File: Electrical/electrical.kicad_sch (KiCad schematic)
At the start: 6 parts, among them SW1 SW_Push

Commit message: Circuit planing
First final version of circuit
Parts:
- added D4: LED, symbol Device:LED
- added M1, M2: Motor_DC, symbol Motor:Motor_DC
- added R2: 10kOhm, symbol Device:R
- added SW2: SW_Push, symbol Switch:SW_Push
- added SW3: SW_DPST_x2, symbol Switch:SW_DPST_x2
- added U1: MPXA6115A, symbol Sensor_Pressure:MPXA6115A
- added U2: L298N, Package_TO_SOT_THT:TO-220-15_P2.54x2.54mm_StaggerOdd_Lead4.58mm_Vertical, symbol Driver_Motor:L298N
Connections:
- net at A1.15 (D0/RX): now also U2.5 (IN1)
- net at A1.16 (D1/TX): now also U2.7 (IN2)
- net at A1.17 (D2): now also U2.10 (IN3)
- net at A1.18 (D3): now also U2.12 (IN4)
- net at A1.19 (D4): now also U2.6 (EnA)
- net at A1.20 (D5): now also U2.11 (EnB)
- net at A1.3 (~{RESET}): now also R2.2, SW2.1
- net at A1.5 (+5V), SW1.2: now also SW2.2, U1.2 (Vcc)
- net at R1.1: now also A1.7 (GND), R2.1, U1.3 (GND); no longer A1.6 (GND)
- net at A1.8 (VIN): now also D4.1 (K)
- net at A1.9 (A0): now also U1.4 (Vout)
- new net: M2.1 (+), U2.13 (OUT3)
- new net: M2.2 (-), U2.14 (OUT4)
- new net: SW3.2 (B), U2.9 (Vss)
- new net: M1.1 (+), U2.2 (OUT1)
- new net: M1.2 (-), U2.3 (OUT2)
- new net: D4.2 (A), U2.4 (Vs)
- new net +BATT: SW3.1 (A)
- new net GND: A1.6 (GND), U2.8 (GND)
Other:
- moved on the sheet: A1, D1, D2, D3, R1, SW1

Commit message: Konverting to Pico
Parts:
- removed A1: Arduino_UNO_R2, Module:Arduino_UNO_R2, symbol MCU_Module:Arduino_UNO_R2
- removed U1: MPXA6115A, symbol Sensor_Pressure:MPXA6115A
- added U1: Pico, RPi_Pico:RPi_Pico_SMD_TH, symbol MCU_RaspberryPi_and_Boards:Pico
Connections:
- net GND: now also U1.13 (GND)
- net at R1.1, R2.1: now also U1.3 (GND)
- net at D1.1 (K), D2.1 (K), D3.1 (K): now also U1.38 (GND)
- net at D3.2 (A): now also U1.26 (GPIO20)
- net at SW1.2, SW2.2: now also U1.36 (3V3)
- net at R1.2, SW1.1: now also U1.21 (GPIO16)
- net at D1.2 (A): now also U1.24 (GPIO18)
- net at D2.2 (A): now also U1.25 (GPIO19)
- net at D4.1 (K): now also U1.39 (VSYS)
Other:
- note added: "Main control circuitry"
- note added: "arduino control circuitry"
- moved on the sheet: D1, D2, D3

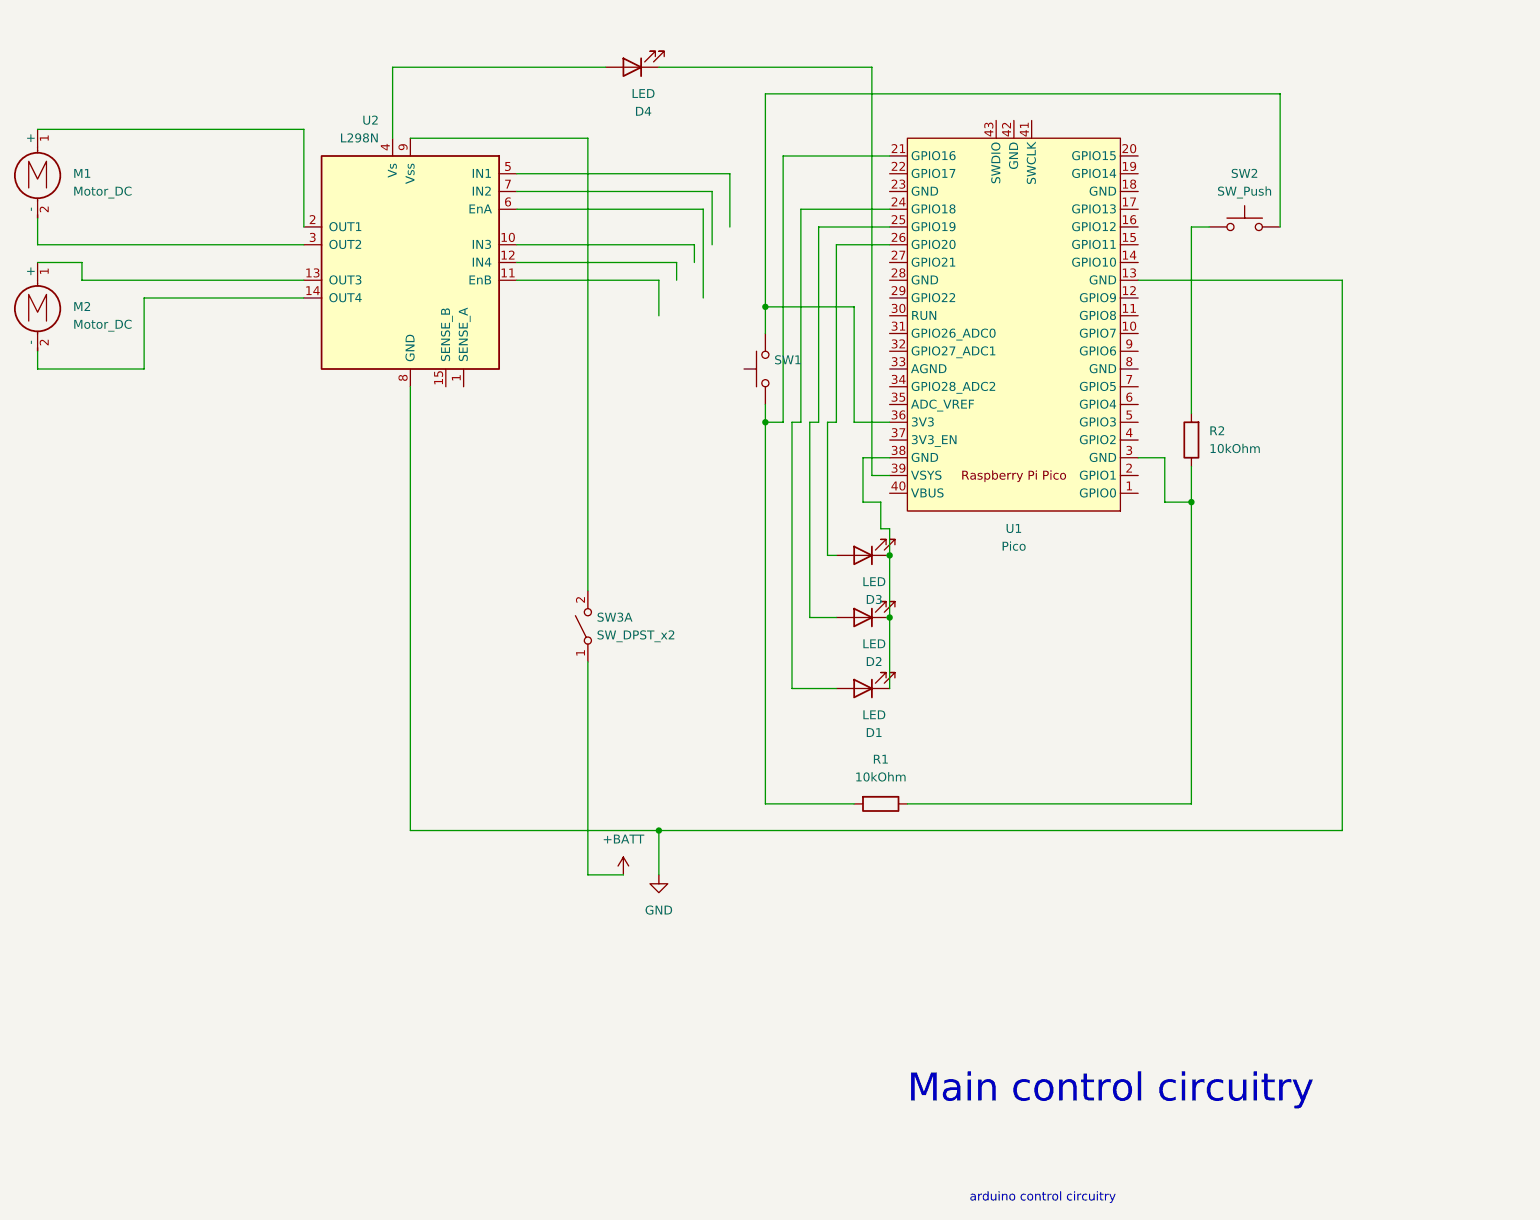
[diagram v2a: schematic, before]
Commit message: converting to a pico
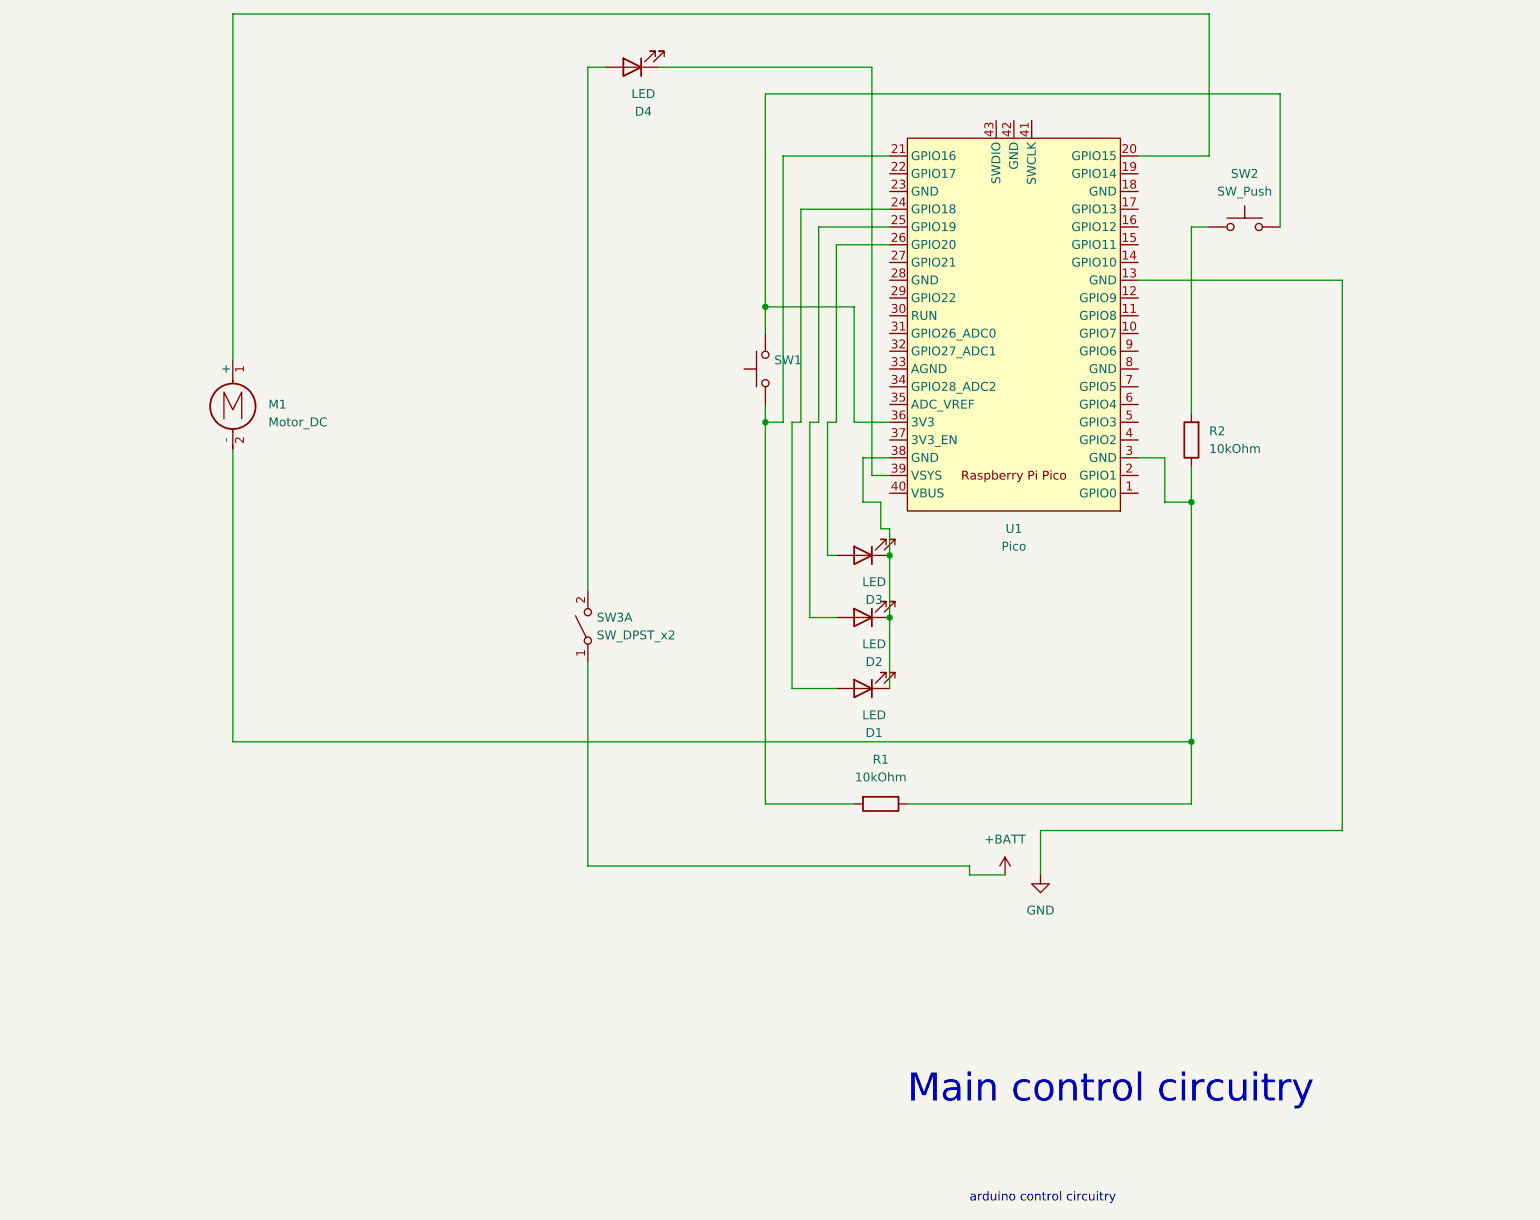
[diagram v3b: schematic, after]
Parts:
- removed M2: Motor_DC, symbol Motor:Motor_DC
- removed U2: L298N, Package_TO_SOT_THT:TO-220-15_P2.54x2.54mm_StaggerOdd_Lead4.58mm_Vertical, symbol Driver_Motor:L298N
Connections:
- net at R1.1, R2.1, U1.3 (GND): now also M1.2 (-)
- net at SW3.2 (B): now also D4.2 (A)
- net at U1.20 (GPIO15): now also M1.1 (+)

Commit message: Intro of Pico Code
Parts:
- added R3, R4, R5: R_Small, symbol Device:R_Small
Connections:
- net at D3.2 (A): now also R3.2; no longer U1.26 (GPIO20)
- net at U1.24 (GPIO18): now also R5.1; no longer D1.2 (A)
- net at U1.25 (GPIO19): now also R4.1; no longer D2.2 (A)
- new net: R3.1, U1.26 (GPIO20)
- new net: D1.2 (A), R5.2
- new net: D2.2 (A), R4.2
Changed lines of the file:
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@@
     (stroke (width 0) (type default))
   )
-  (wire (pts (xy 165.1 78.74) (xy 165.1 106.68))
+  (wire (pts (xy 165.1 78.74) (xy 165.1 100.33))
     (stroke (width 0) (type default))
   )
@@
     (stroke (width 0) (type default))
   )
-  (wire (pts (xy 167.64 78.74) (xy 167.64 97.79))
+  (wire (pts (xy 167.64 78.74) (xy 167.64 90.17))
     (stroke (width 0) (type default))
   )
@@
     (stroke (width 0) (type default))
   )
+  (wire (pts (xy 167.64 95.25) (xy 167.64 97.79))
+    (stroke (width 0) (type default))
+  )
   (wire (pts (xy 165.1 78.74) (xy 166.37 78.74))
     (stroke (width 0) (type default))
@@
     (stroke (width 0) (type default))
   )
-  (wire (pts (xy 162.56 78.74) (xy 162.56 116.84))
+  (wire (pts (xy 162.56 78.74) (xy 162.56 109.22))
+    (stroke (width 0) (type default))
+  )
+  (wire (pts (xy 165.1 105.41) (xy 165.1 106.68))
     (stroke (width 0) (type default))
   )
@@
   )
   (wire (pts (xy 193.04 143.51) (xy 187.96 143.51))
+    (stroke (width 0) (type default))
+  )
+  (wire (pts (xy 162.56 114.3) (xy 162.56 116.84))
     (stroke (width 0) (type default))
   )
@@
         )
       )
+    )
+  )
+  (symbol (lib_id "Device:R_Small") (at 167.64 92.71 0) (unit 1)
+    (in_bom yes) (on_board yes) (dnp no) (fields_autoplaced)
+    (property "Reference" "R3" (at 170.18 91.44 0)
+      (effects (font (size 1.27 1.27)) (justify left))
+    )
+    (property "Value" "R_Small" (at 170.18 93.98 0)
+      (effects (font (size 1.27 1.27)) (justify left))
+    )
+    (property "Footprint" "" (at 167.64 92.71 0)
+      (effects (font (size 1.27 1.27)) hide)
+    )
+    (property "Datasheet" "~" (at 167.64 92.71 0)
+      (effects (font (size 1.27 1.27)) hide)
+    )
+    (pin "1")
+    (pin "2")
+    (instances
+      (project "electrical"
+        (path "/a8f1ef9d-ede4-4b5c-88d3-ab957278c1f8"
+          (reference "R3") (unit 1)
+        )
+      )
+    )
+  )
+  (symbol (lib_id "Device:R_Small") (at 162.56 111.76 0) (unit 1)
+    (in_bom yes) (on_board yes) (dnp no) (fields_autoplaced)
+    (property "Reference" "R5" (at 165.1 110.49 0)
+      (effects (font (size 1.27 1.27)) (justify left))
+    )
+    (property "Value" "R_Small" (at 165.1 113.03 0)
+      (effects (font (size 1.27 1.27)) (justify left))
+    )
+    (property "Footprint" "" (at 162.56 111.76 0)
+      (effects (font (size 1.27 1.27)) hide)
+    )
+    (property "Datasheet" "~" (at 162.56 111.76 0)
+      (effects (font (size 1.27 1.27)) hide)
+    )
+    (pin "1")
+    (pin "2")
+    (instances
+      (project "electrical"
+        (path "/a8f1ef9d-ede4-4b5c-88d3-ab957278c1f8"
+          (reference "R5") (unit 1)
+        )
+      )
+    )
+  )
+  (symbol (lib_id "Device:R_Small") (at 165.1 102.87 0) (unit 1)
+    (in_bom yes) (on_board yes) (dnp no) (fields_autoplaced)
+    (property "Reference" "R4" (at 167.64 101.6 0)
+      (effects (font (size 1.27 1.27)) (justify left))
+    )
+    (property "Value" "R_Small" (at 167.64 104.14 0)
+      (effects (font (size 1.27 1.27)) (justify left))
+    )
+    (property "Footprint" "" (at 165.1 102.87 0)
+      (effects (font (size 1.27 1.27)) hide)
+    )
+    (property "Datasheet" "~" (at 165.1 102.87 0)
+      (effects (font (size 1.27 1.27)) hide)
+    )
+    (pin "1")
+    (pin "2")
+    (instances
+      (project "electrical"
+        (path "/a8f1ef9d-ede4-4b5c-88d3-ab957278c1f8"
+          (reference "R4") (unit 1)
+        )
+      )

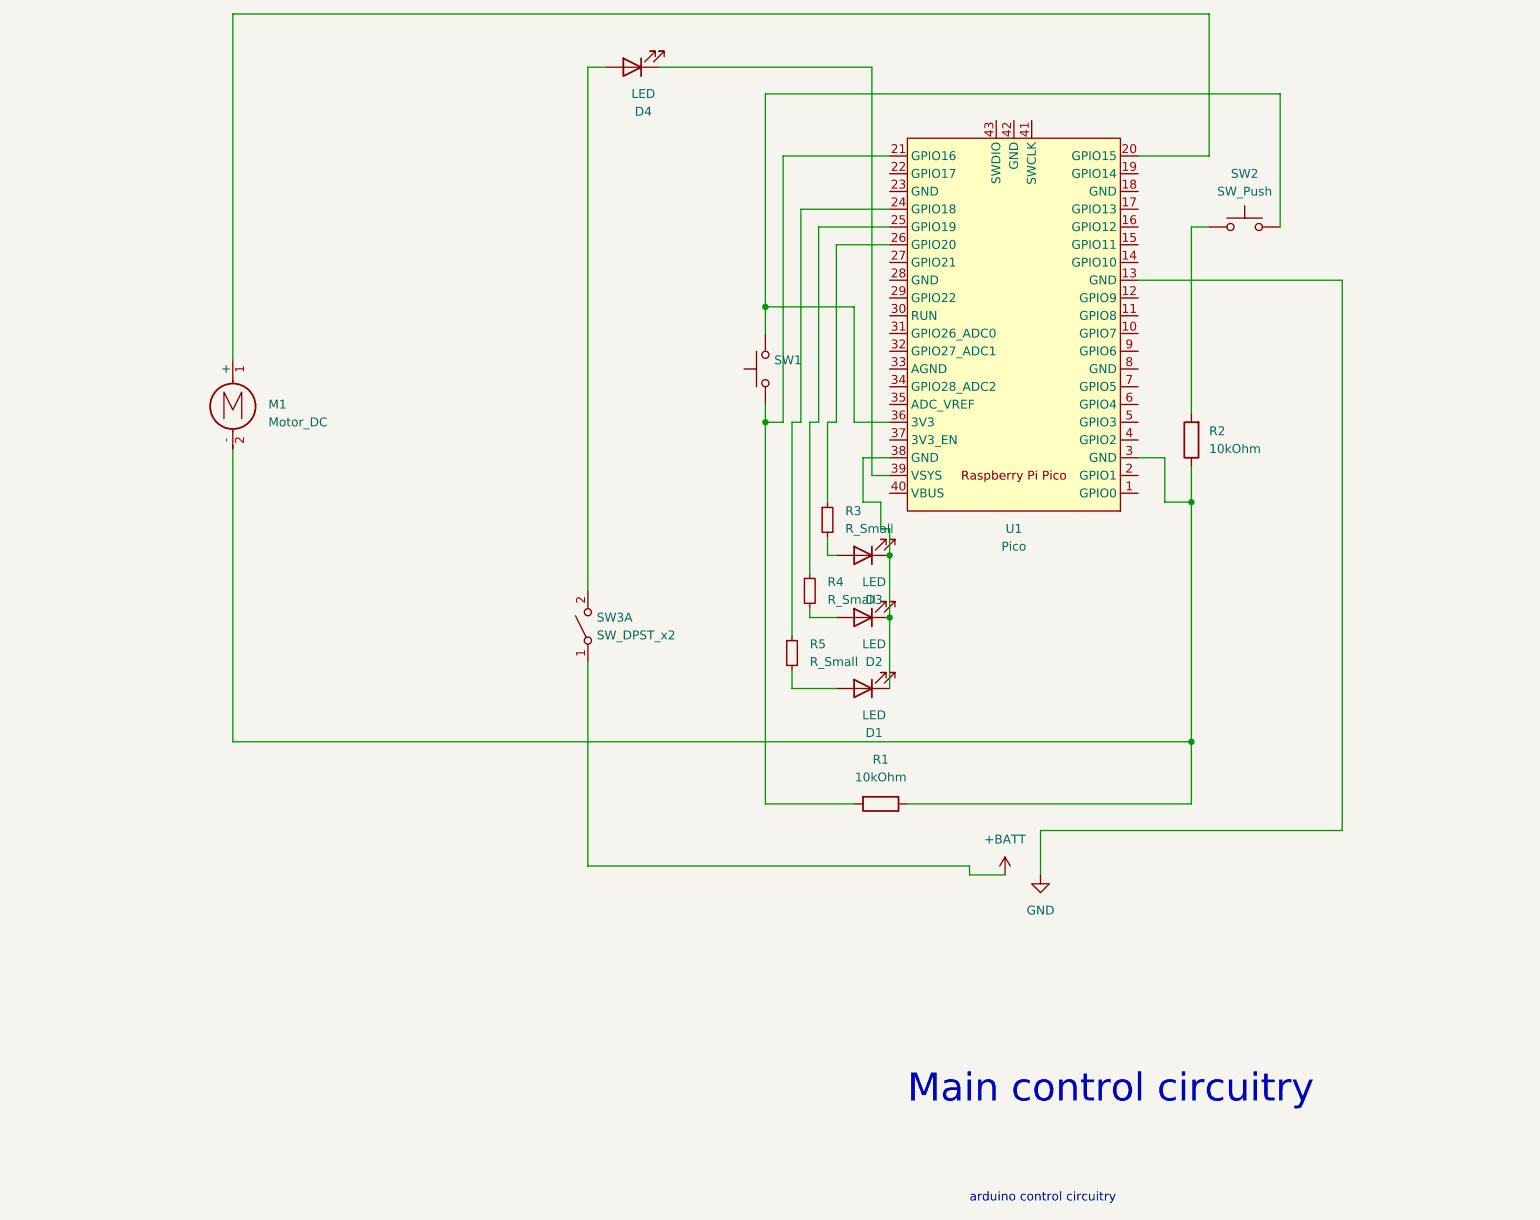
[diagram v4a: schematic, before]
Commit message: switching to servo
switching to servo in the plans
adding code for programming mode
adding code for arming and programming
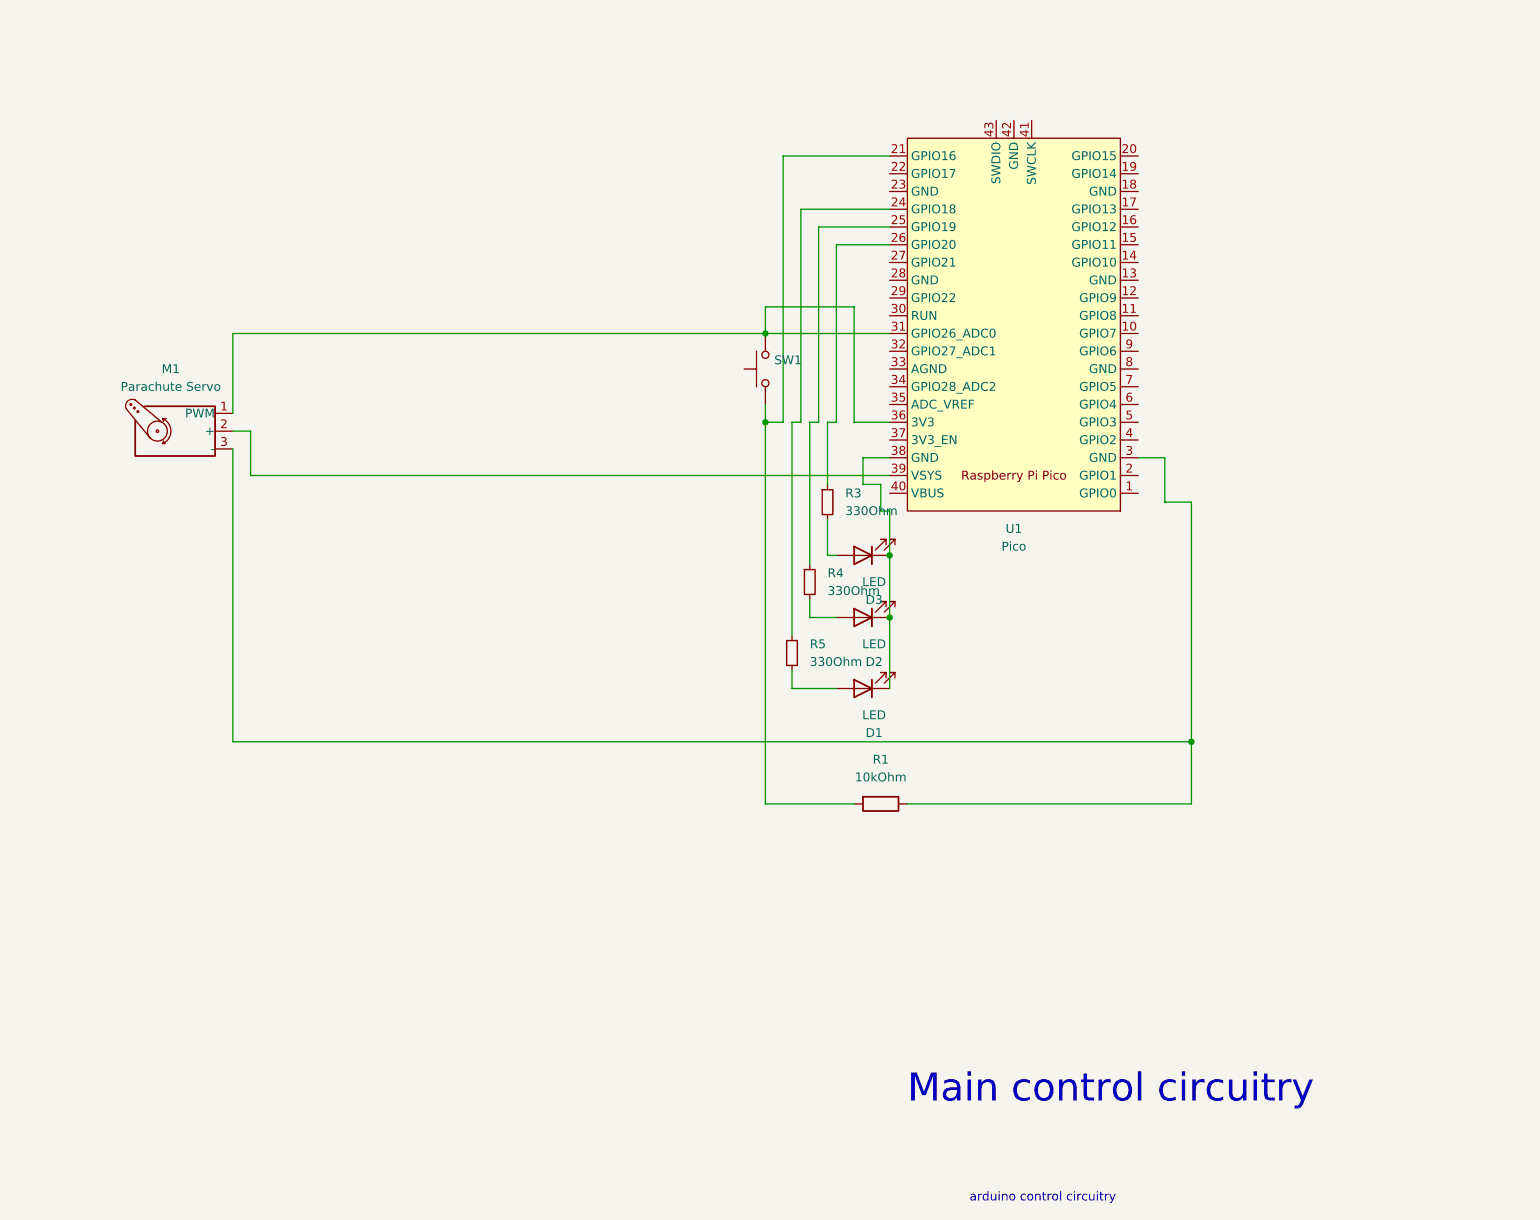
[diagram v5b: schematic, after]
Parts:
- removed D4: LED, symbol Device:LED
- removed M1: Motor_DC, symbol Motor:Motor_DC
- removed R2: 10kOhm, symbol Device:R
- removed SW2: SW_Push, symbol Switch:SW_Push
- removed SW3: SW_DPST_x2, symbol Switch:SW_DPST_x2
- added M1: Parachute Servo, symbol Motor:Motor_Servo
- R3, R4, R5: value R_Small -> 330Ohm
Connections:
- net at R1.1, U1.3 (GND): now also M1.3 (-)
- net at U1.31 (GPIO26_ADC0): now also SW1.2, U1.36 (3V3), M1.1 (PWM)
- net at U1.39 (VSYS): now also M1.2 (+)
- net GND: no longer names the net of U1.13 (GND)
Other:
- moved on the sheet: R3, R4
